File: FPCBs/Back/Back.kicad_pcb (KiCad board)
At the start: 2 copper layers, 125.7 x 88.4 mm, 23 parts, among them J1 To PCB, J2 To Front, J3 Front, J4 EVF_SENSOR, J5 From LCD, SW1 MENU/SET, SW10 -+-, SW11 PLAY, SW13 S/C/M, SW14 SCREEN_OFF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

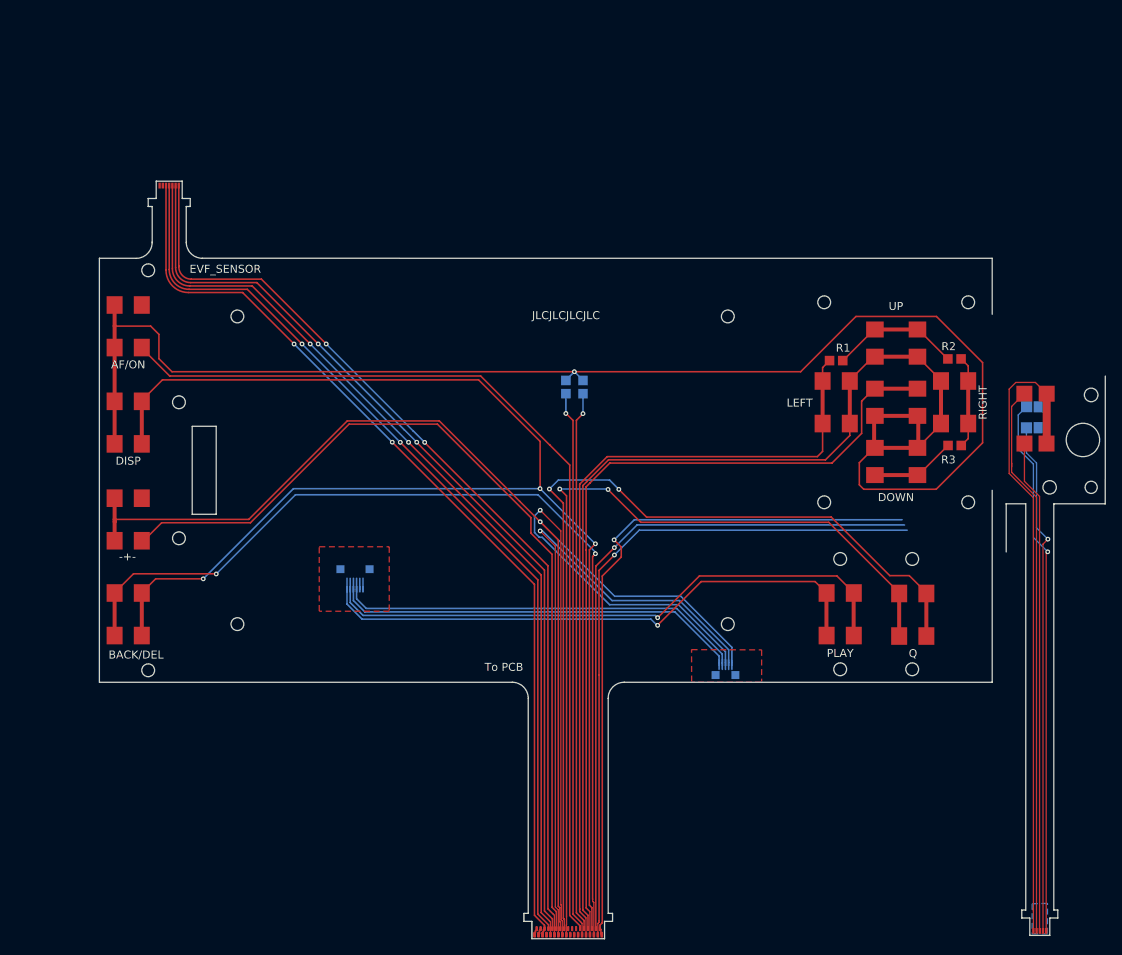
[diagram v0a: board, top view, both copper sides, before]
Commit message: Add EVF optocoupler
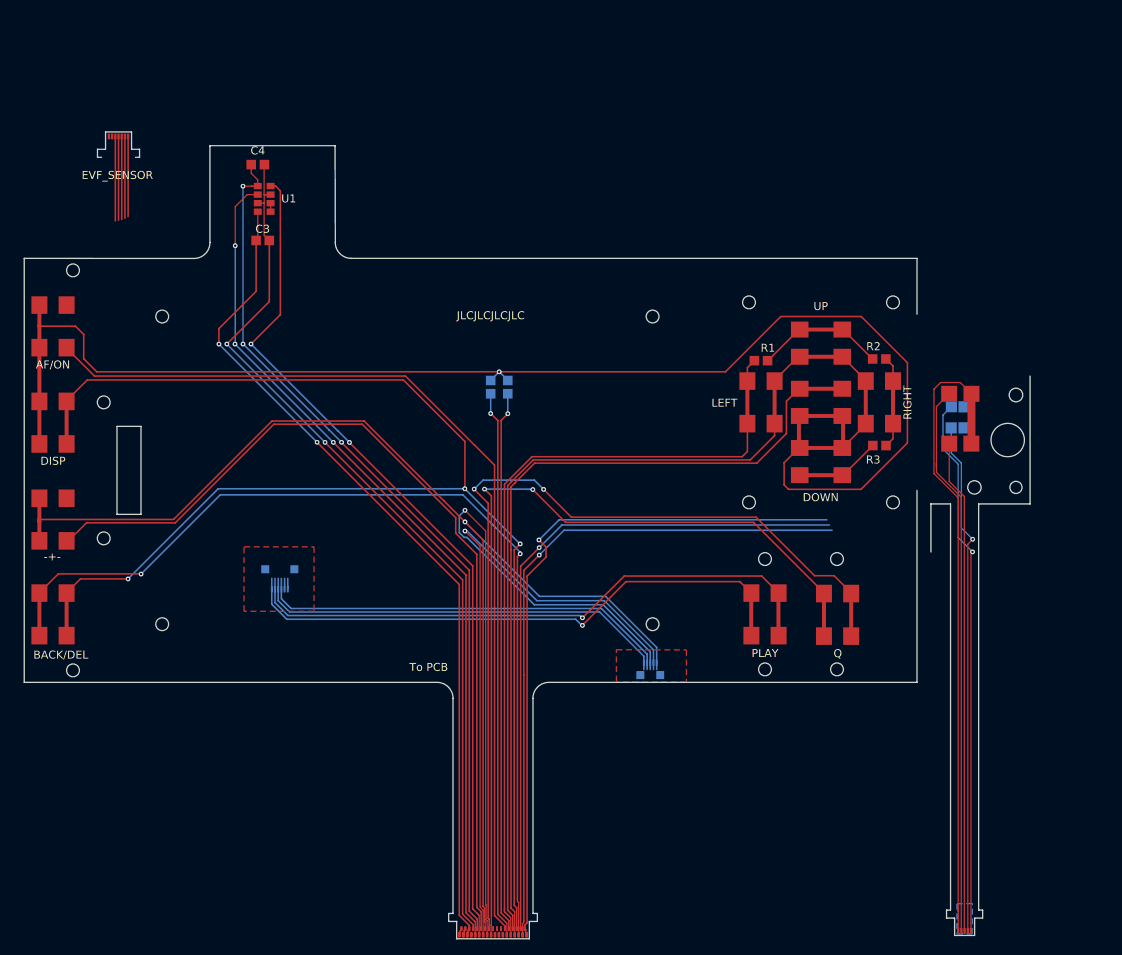
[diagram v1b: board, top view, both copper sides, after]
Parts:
- added C3: C, Leica-G9ii:R_0603, F.Cu at (79.8, 47.8)
- added C4: C, Leica-G9ii:R_0603, F.Cu at (79.2, 38.3)
- added U1: 6N137, Leica-G9ii:Optocoupler_EVF, F.Cu at (80.0, 42.6)
- moved J1 9.40 mm to (108.6, 133.1)
- moved J2 9.40 mm to (128.3, 101.5)
- moved R1 9.40 mm to (142.1, 62.8)
- moved R2 9.40 mm to (156.9, 62.6)
- moved R3 9.40 mm to (156.9, 73.4)
- moved SW1 9.40 mm to (149.6, 68.0)
- moved SW11 9.40 mm to (142.6, 94.5)
- moved SW13 9.40 mm to (169.8, 70.0)
- moved SW14 9.40 mm to (168.2, 69.9)
- moved SW2 9.40 mm to (156.9, 68.0)
- moved SW3 9.40 mm to (149.6, 75.4)
- moved SW4 9.40 mm to (142.1, 68.0)
- moved SW5 9.40 mm to (149.6, 60.6)
- moved SW7 9.40 mm to (151.7, 94.6)
- moved SW10 9.40 mm to (53.6, 82.7)
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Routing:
- net Net-(J1-Pin_7): track 117.1 -> 123.6 mm
- net Net-(J1-Pin_10): track 117.5 -> 120.1 mm, vias 2 -> 3
- net Net-(J1-Pin_5): track 117.6 -> 116.0 mm
- net Net-(U1-EN): track 0.00 -> 1.07 mm
- net Net-(J1-Pin_9): track 118.1 -> 117.3 mm, vias 2 -> 3
- net Net-(J1-Pin_11): track 118.4 -> 117.8 mm
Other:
- board size 125.7 x 88.4 mm -> 125.7 x 96 mm

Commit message: Fix positions on back fpcb
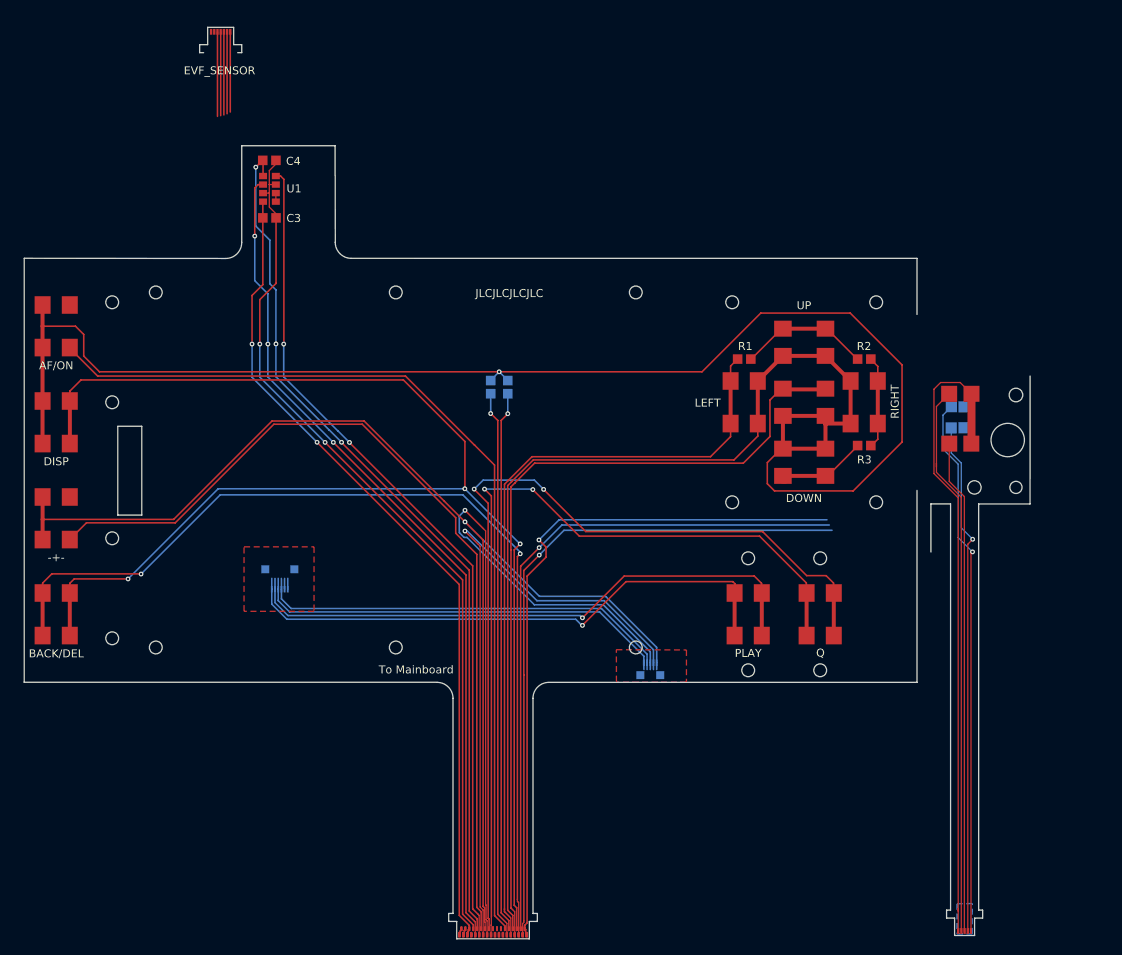
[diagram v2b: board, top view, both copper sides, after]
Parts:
- J1: value To PCB -> To Mainboard
- moved J4 18.3 mm to (74.6, 23.1)
- moved C3 2.94 mm to (80.7, 45.0)
- moved SW7 2.17 mm to (149.5, 94.5)
- moved SW5 2.10 mm to (147.5, 60.5)
- moved SW3 2.10 mm to (147.5, 75.5)
- moved SW1 2.10 mm to (147.5, 68.0)
- moved SW11 2.10 mm to (140.5, 94.5)
- moved SW4 2.10 mm to (140.0, 68.0)
- moved R1 2.10 mm to (140.0, 62.6)
- moved SW2 1.90 mm to (155.0, 68.0)
- moved R3 1.90 mm to (155.0, 73.4)
- moved R2 1.88 mm to (155.0, 62.6)
- moved C4 1.54 mm to (80.7, 37.8)
- moved U1 1.42 mm to (80.7, 41.3)
- moved SW10 0.43 mm to (54.0, 82.5)
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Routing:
- net Net-(J1-Pin_7): track 123.6 -> 120.2 mm
- net Net-(J1-Pin_27): track 100.4 -> 97.9 mm
- net Net-(J1-Pin_11): track 117.8 -> 115.8 mm
- net Net-(J1-Pin_28): track 313.1 -> 311.0 mm
- net Net-(J1-Pin_5): track 116.0 -> 114.1 mm
- net Net-(J1-Pin_17): track 109.7 -> 107.8 mm
- net Net-(J1-Pin_29): track 105.2 -> 103.3 mm
- net Net-(J1-Pin_16): track 114.7 -> 113.3 mm
- net Net-(J5-Pin_2): track 75.3 -> 74.0 mm
- net Net-(J5-Pin_1): track 72.7 -> 71.4 mm
- net Net-(J1-Pin_9): track 117.3 -> 116.4 mm
- net Net-(SW5A-D): track 16.3 -> 15.5 mm
- net Net-(J1-Pin_14): track 154.2 -> 153.6 mm
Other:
- outline, holes or cut-outs redrawn

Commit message: Improve the back fpcb
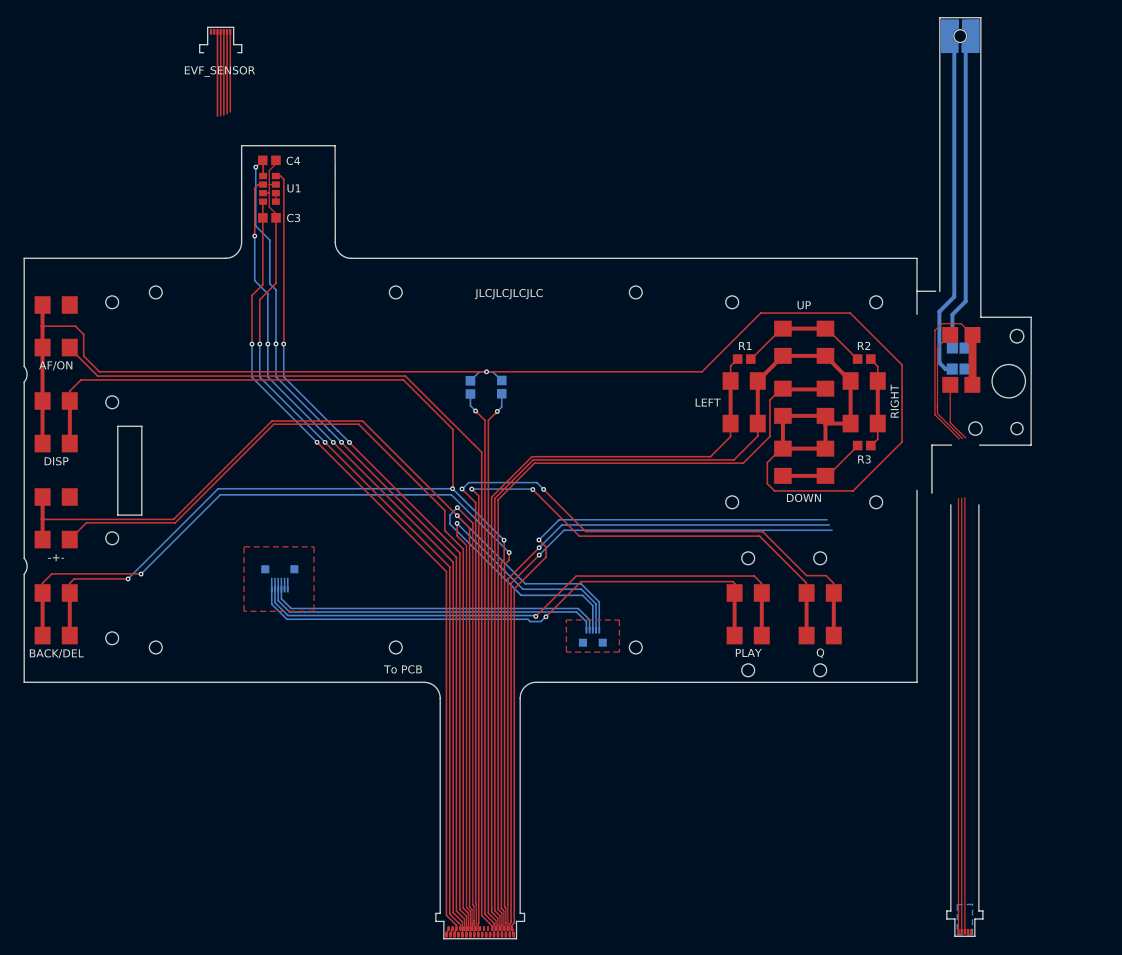
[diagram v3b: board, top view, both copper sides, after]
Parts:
- added J6: To Right, Leica-G9ii:Connector-Screw-2Pins, B.Cu at (167.0, 22.2)
- J1: value To Mainboard -> To PCB
- SW14: value SCREEN_OFF -> ON/OFF
- moved J2 8.25 mm to (121.1, 97.4)
- moved SW13 7.35 mm to (170.0, 62.7)
- moved SW14 7.35 mm to (168.3, 62.5)
- moved C1 2.53 mm to (105.8, 66.1)
- moved J1 1.60 mm to (107.0, 133.1)
- moved C2 0.75 mm to (109.7, 66.1)
- moved J3 0.12 mm to (167.6, 132.8)
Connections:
- J3 pad 4: Net-(J3-Pin_4) -> unconnected-(J3-Pin_4-Pad4)
- J3 pad 5: Net-(J3-Pin_5) -> unconnected-(J3-Pin_5-Pad5)
- SW14 pad 1: Net-(J3-Pin_4) -> Net-(J6-Pin_1)
- SW14 pad 2: Net-(J3-Pin_5) -> Net-(J6-Pin_2)
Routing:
- net Net-(J3-Pin_5): track 67.6 -> 0.00 mm, vias 1 -> 0
- net Net-(J3-Pin_4): track 64.3 -> 0.00 mm, vias 1 -> 0
- net Net-(J6-Pin_1): track 0.00 -> 43.9 mm
- net Net-(J6-Pin_2): track 0.00 -> 40.1 mm
- net Net-(J2-Pin_5): track 53.0 -> 43.5 mm
- net Net-(J2-Pin_4): track 53.0 -> 43.5 mm
- net Net-(J1-Pin_14): track 153.6 -> 145.3 mm
- net Net-(J1-Pin_15): track 89.5 -> 82.5 mm
- net Net-(J1-Pin_13): track 83.6 -> 76.9 mm
- net Net-(J1-Pin_28): track 311.0 -> 313.5 mm
- net Net-(J1-Pin_30): track 185.0 -> 182.5 mm
- net Net-(J1-Pin_17): track 107.8 -> 109.4 mm
- net Net-(J1-Pin_31): track 121.8 -> 120.5 mm
- net Net-(J1-Pin_16): track 113.3 -> 114.5 mm
- net Net-(J1-Pin_12): track 112.1 -> 111.2 mm
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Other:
- board size 125.7 x 96 mm -> 125.9 x 112 mm

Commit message: Add front lever flex cable
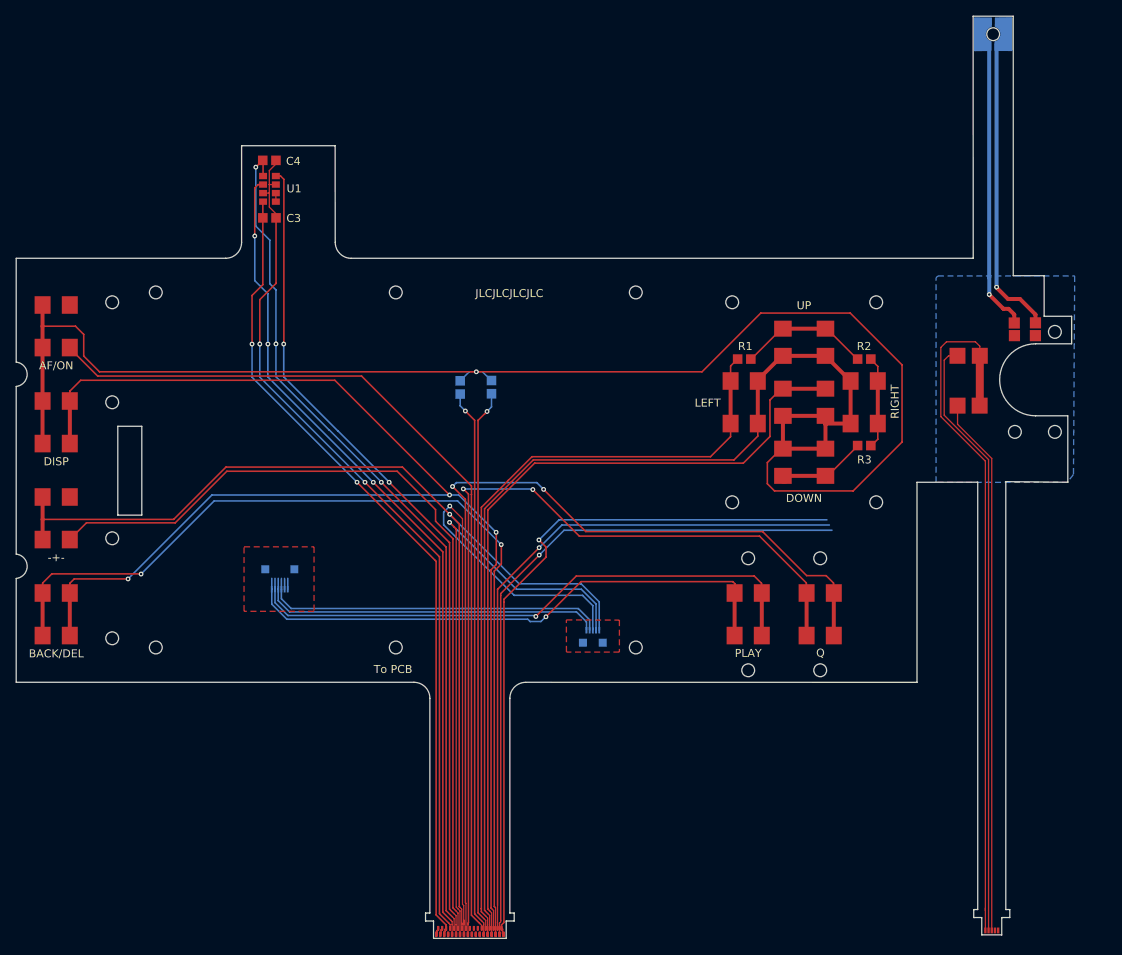
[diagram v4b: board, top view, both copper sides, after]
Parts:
- removed J4: EVF_SENSOR, Leica-G9ii:FPC-1Row-7Pins-0.40mm
- SW14: moved to F.Cu
- moved SW14 7.08 mm to (175.1, 60.4), turned to 180 degrees
- moved J6 4.12 mm to (171.1, 22.0), turned to 90 degrees
- moved J3 3.36 mm to (170.9, 132.6)
- moved SW13 2.75 mm to (170.9, 65.3)
- moved J1 1.29 mm to (105.7, 133.1)
- moved C1 1.28 mm to (104.5, 66.1)
- moved C2 1.28 mm to (108.4, 66.1)
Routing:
- net Net-(J1-Pin_5): track 113.5 -> 102.3 mm
- net Net-(J1-Pin_7): track 119.5 -> 108.5 mm
- net Net-(J1-Pin_9): track 115.7 -> 104.7 mm
- net Net-(J1-Pin_10): track 119.5 -> 108.6 mm
- net Net-(J1-Pin_11): track 115.1 -> 104.5 mm
- net Net-(J3-Pin_1): track 81.2 -> 88.3 mm
- net Net-(J1-Pin_12): track 111.2 -> 105.1 mm
- net Net-(J3-Pin_2): track 69.6 -> 75.5 mm
- net Net-(J3-Pin_3): track 61.7 -> 67.4 mm
- net Net-(J1-Pin_30): track 182.5 -> 177.0 mm
- net Net-(J1-Pin_14): track 145.3 -> 140.5 mm
- net Net-(J6-Pin_1): track 43.9 -> 39.5 mm, vias 0 -> 1
- net Net-(J1-Pin_24): track 117.2 -> 113.4 mm
- net Net-(J6-Pin_2): track 40.1 -> 37.7 mm, vias 0 -> 1
- net Net-(J1-Pin_16): track 114.5 -> 115.8 mm
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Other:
- board size 125.9 x 112 mm -> 131.9 x 112.1 mm

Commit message: Fix switch detectors footprints
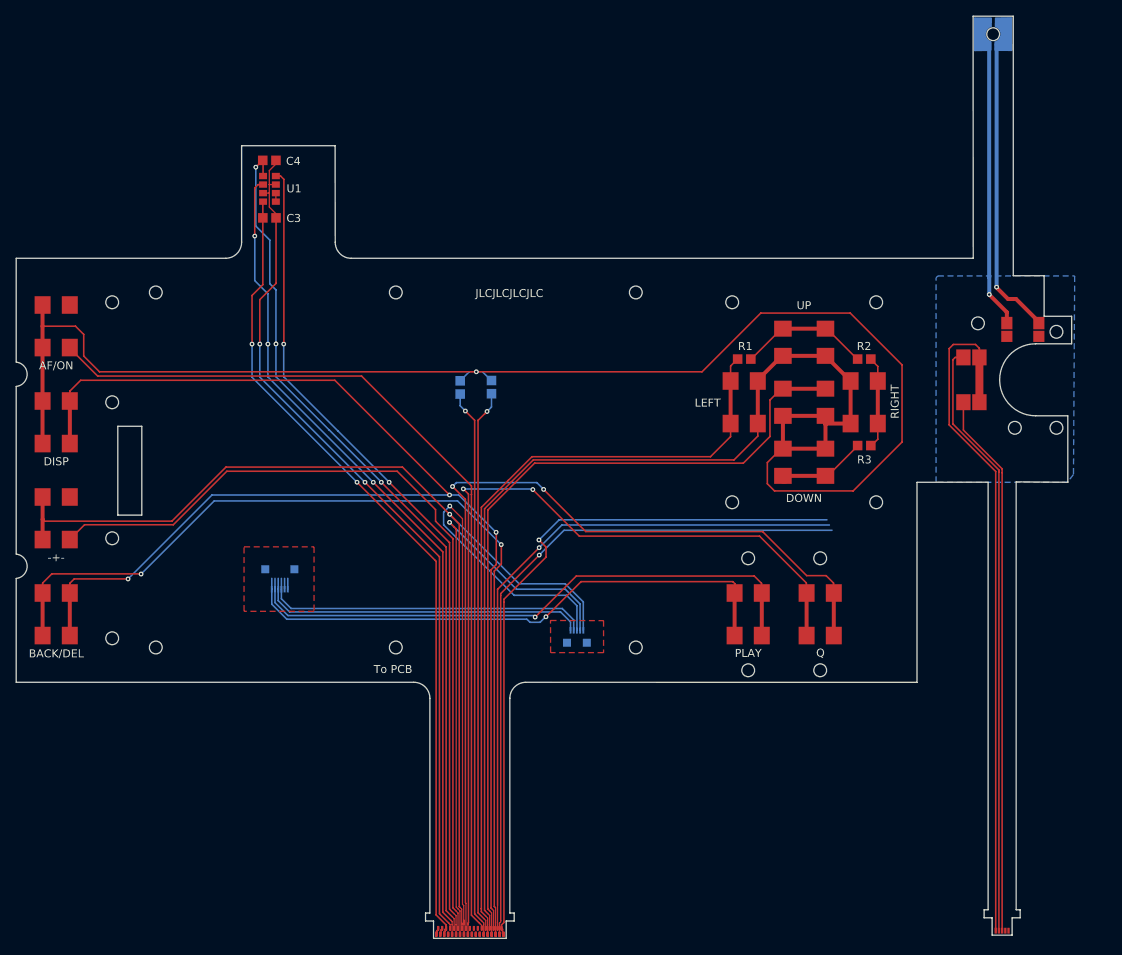
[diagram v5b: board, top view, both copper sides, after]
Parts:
- moved J2 1.99 mm to (119.1, 97.4)
- moved SW13 1.68 mm to (169.2, 65.2)
- moved SW14 1.46 mm to (174.8, 59.0)
- moved J3 1.30 mm to (172.2, 132.7)
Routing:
- net Net-(J3-Pin_1): track 88.3 -> 86.1 mm
- net Net-(J2-Pin_4): track 43.5 -> 41.5 mm
- net Net-(J1-Pin_13): track 77.9 -> 75.9 mm
- net Net-(J2-Pin_5): track 43.5 -> 41.5 mm
- net Net-(J1-Pin_15): track 83.4 -> 81.4 mm
- net Net-(J1-Pin_14): track 140.5 -> 138.7 mm
- net Net-(J6-Pin_2): track 37.7 -> 36.9 mm
- net Net-(J3-Pin_3): track 67.4 -> 68.1 mm
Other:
- outline, holes or cut-outs redrawn
